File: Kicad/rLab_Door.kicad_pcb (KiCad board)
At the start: 4 copper layers, 100 x 100 mm, 96 parts, among them J1 ACT_1, J10 BATTERY, J11 PROG, J12 PI, J13 TEST POINTS, J2 ACT_2, J3 NPX_1, J4 NPX_2, J5 WIEGAND KEYPAD, J6 NFC SERIAL, J7 I2C DISPLAY, J8 TAMPER, J9 V_IN, Q1 2N7002, Q10 MMBT5551L, Q11 2N7002, Q12 2N7002, Q2 2N7002, Q3 AO3401A, Q4 MMBT5551L, Q5 2N7002, Q6 2N7002, Q7 AO3401A, Q8 2N7002, Q9 2N7002, SW1 RESET, SW2 BOOT, SW3 TEST_1, SW4 TEST_2, U1 MP1584, U2 LM317_TO-252, U3 AMS1117-3.3, U4 ESP32-WROOM-32D

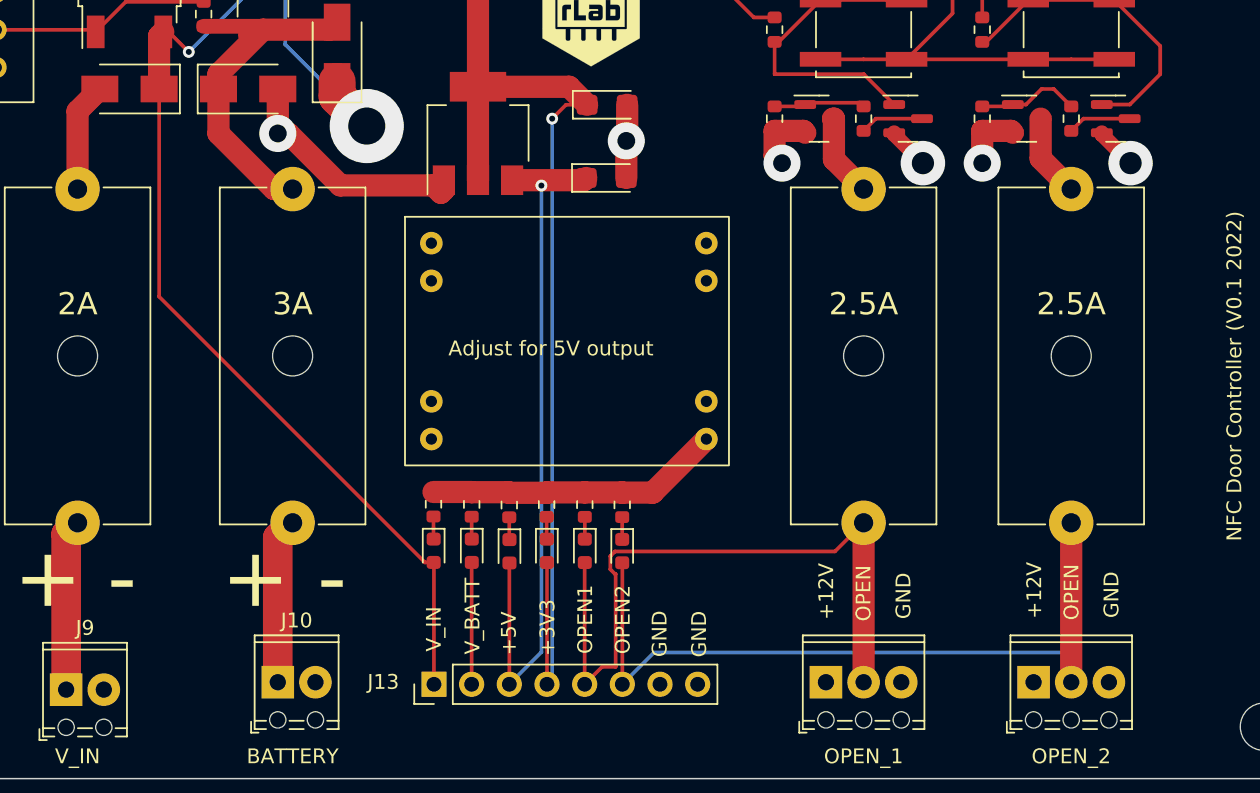
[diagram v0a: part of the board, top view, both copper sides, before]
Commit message: Added some vias to the high power connections to improve current capacity
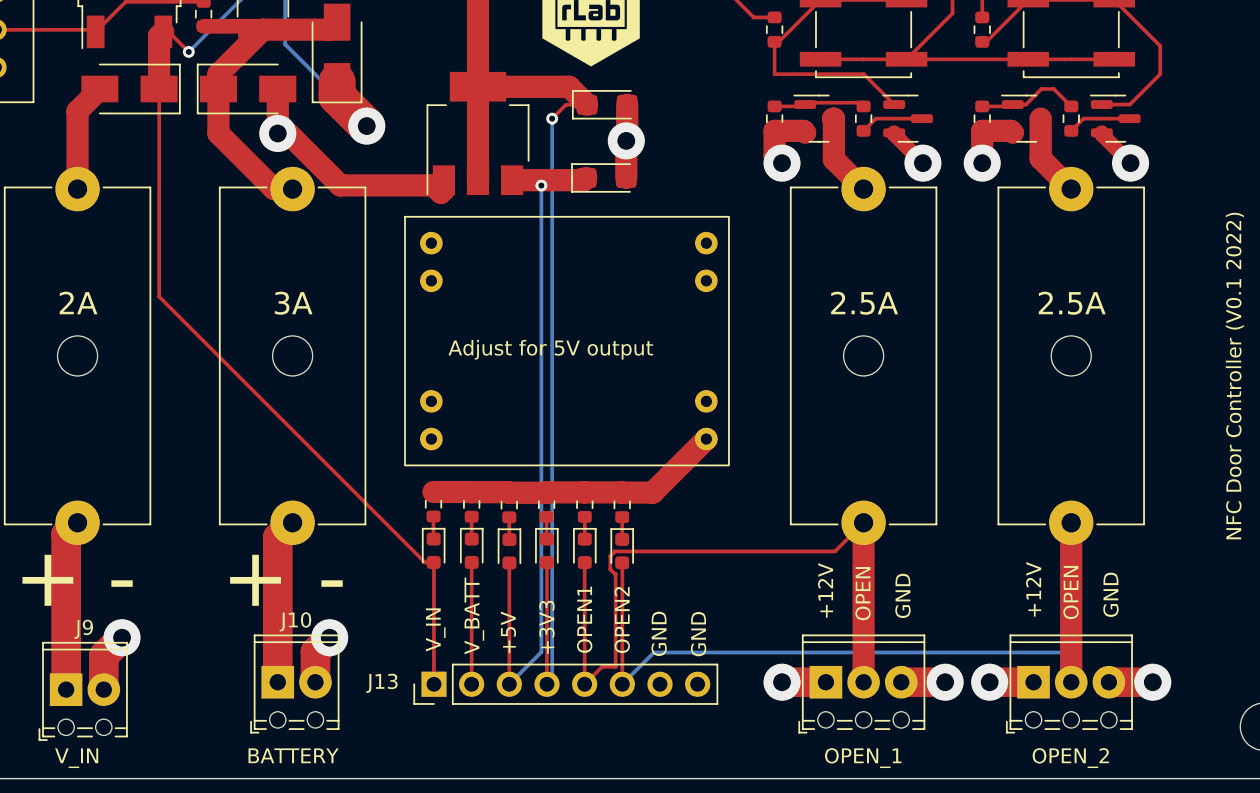
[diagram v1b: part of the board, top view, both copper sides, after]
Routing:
- net GND: track 102.3 -> 115.6 mm, vias 12 -> 16
- net +BATT: track 62.8 -> 68.7 mm, vias 4 -> 6
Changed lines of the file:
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@@
   (segment (start 84.325 67.254176) (end 85.745824 67.254176) (width 0.25) (layer "F.Cu") (net 2))
   (segment (start 89.560842 127.175) (end 89.574391 127.188549) (width 1.5) (layer "F.Cu") (net 2))
+  (segment (start 79.04 137.96) (end 80 137) (width 2) (layer "F.Cu") (net 2))
   (segment (start 76.5 100) (end 76.5 103) (width 1.5) (layer "F.Cu") (net 2))
   (segment (start 100 106) (end 100 103.5) (width 1.5) (layer "F.Cu") (net 2))
@@
   (segment (start 114 56.9) (end 114 59) (width 0.25) (layer "F.Cu") (net 2))
   (segment (start 76.5 103) (end 77.214824 103) (width 1.5) (layer "F.Cu") (net 2))
+  (segment (start 132.54 140) (end 135.5 140) (width 2) (layer "F.Cu") (net 2))
   (segment (start 87.5 107) (end 87.7 106.8) (width 1.5) (layer "F.Cu") (net 2))
   (segment (start 84.25 60.155) (end 88.28 60.155) (width 0.25) (layer "F.Cu") (net 2))
   (segment (start 83.915 59.87) (end 83.94 59.845) (width 0.25) (layer "F.Cu") (net 2))
   (segment (start 91.065 77.665) (end 91.065 75.565) (width 0.25) (layer "F.Cu") (net 2))
+  (segment (start 118.54 140) (end 121.5 140) (width 2) (layer "F.Cu") (net 2))
   (segment (start 100.057332 101.065037) (end 100.057332 103.442668) (width 1.5) (layer "F.Cu") (net 2))
   (segment (start 118.0625 103.0625) (end 120 105) (width 1) (layer "F.Cu") (net 2))
@@
   (segment (start 84.33535 69) (end 86 69) (width 0.25) (layer "F.Cu") (net 2))
   (segment (start 75.835 51.28) (end 75.835 57.08) (width 0.25) (layer "F.Cu") (net 2))
+  (segment (start 64.77 140.5) (end 64.77 138.23) (width 2) (layer "F.Cu") (net 2))
   (segment (start 85.268167 70.768152) (end 85.512299 70.52402) (width 0.25) (layer "F.Cu") (net 2))
   (segment (start 114 59) (end 113 60) (width 0.25) (layer "F.Cu") (net 2))
@@
   (segment (start 99.722911 127.215648) (end 101.786352 127.215648) (width 1.5) (layer "F.Cu") (net 2))
   (segment (start 87 127.175) (end 89.560842 127.175) (width 1.5) (layer "F.Cu") (net 2))
+  (segment (start 79.04 140) (end 79.04 137.96) (width 2) (layer "F.Cu") (net 2))
   (segment (start 99.709362 127.202099) (end 99.722911 127.215648) (width 1.5) (layer "F.Cu") (net 2))
   (segment (start 87 106.5) (end 87.5 107) (width 1.5) (layer "F.Cu") (net 2))
@@
   (segment (start 101.786352 127.215648) (end 105.398 123.604) (width 1.5) (layer "F.Cu") (net 2))
   (segment (start 74.72 51.28) (end 74 52) (width 0.25) (layer "F.Cu") (net 2))
+  (segment (start 64.77 138.23) (end 66 137) (width 2) (layer "F.Cu") (net 2))
   (segment (start 105.28 60.155) (end 112.845 60.155) (width 0.25) (layer "F.Cu") (net 2))
   (segment (start 89.574391 127.188549) (end 92.067485 127.188549) (width 1.5) (layer "F.Cu") (net 2))
@@
   (segment (start 81.94 59.87) (end 80.13 59.87) (width 0.25) (layer "F.Cu") (net 2))
   (segment (start 75.835 58.61) (end 77.225 60) (width 0.25) (layer "F.Cu") (net 2))
+  (via (at 66 137) (size 2.5) (drill 1.2) (layers "F.Cu" "B.Cu") (net 2))
   (via (at 113 60) (size 0.8) (drill 0.4) (layers "F.Cu" "B.Cu") (net 2))
+  (via (at 135.5 140) (size 2.5) (drill 1.2) (layers "F.Cu" "B.Cu") (net 2))
+  (via (at 121.5 140) (size 2.5) (drill 1.2) (layers "F.Cu" "B.Cu") (net 2))
   (via (at 91 75.5) (size 0.8) (drill 0.4) (layers "F.Cu" "B.Cu") (net 2))
   (via (at 86 69) (size 0.8) (drill 0.4) (layers "F.Cu" "B.Cu") (net 2))
   (via (at 74 52) (size 0.8) (drill 0.4) (layers "F.Cu" "B.Cu") (net 2))
-  (via (at 120 105) (size 3) (drill 1.5) (layers "F.Cu" "B.Cu") (net 2))
+  (via (at 120 105) (size 2.5) (drill 1.2) (layers "F.Cu" "B.Cu") (net 2))
   (via (at 86 67) (size 0.8) (drill 0.4) (layers "F.Cu" "B.Cu") (net 2))
   (via (at 85.512299 70.52402) (size 0.8) (drill 0.4) (layers "F.Cu" "B.Cu") (net 2))
   (via (at 80 60) (size 0.8) (drill 0.4) (layers "F.Cu" "B.Cu") (net 2))
-  (via (at 134 105) (size 3) (drill 1.5) (layers "F.Cu" "B.Cu") (net 2))
+  (via (at 134 105) (size 2.5) (drill 1.2) (layers "F.Cu" "B.Cu") (net 2))
+  (via (at 80 137) (size 2.5) (drill 1.2) (layers "F.Cu" "B.Cu") (net 2))
   (via (at 76.5 103) (size 2.5) (drill 1.2) (layers "F.Cu" "B.Cu") (net 2))
   (via (at 100 103.5) (size 2.5) (drill 1.2) (layers "F.Cu" "B.Cu") (net 2))
@@
   (segment (start 125.9375 102.825) (end 126.0625 102.95) (width 1.5) (layer "F.Cu") (net 6))
   (segment (start 110 102.825) (end 111.9375 102.825) (width 1.5) (layer "F.Cu") (net 6))
+  (segment (start 113.46 140) (end 110.5 140) (width 2) (layer "F.Cu") (net 6))
   (segment (start 110 102.825) (end 110 104.5) (width 1.5) (layer "F.Cu") (net 6))
   (segment (start 110 104.5) (end 110.5 105) (width 1.5) (layer "F.Cu") (net 6))
@@
   (segment (start 124 102.825) (end 124 105) (width 1.5) (layer "F.Cu") (net 6))
   (segment (start 89.571669 131.931695) (end 89.571669 140.137882) (width 0.25) (layer "F.Cu") (net 6))
+  (segment (start 127.46 140) (end 124.5 140) (width 2) (layer "F.Cu") (net 6))
   (via (at 77 65.5) (size 0.8) (drill 0.4) (layers "F.Cu" "B.Cu") (net 6))
-  (via (at 82.5 102.5) (size 5) (drill 2.5) (layers "F.Cu" "B.Cu") (net 6))
+  (via (at 82.5 102.5) (size 2.5) (drill 1.2) (layers "F.Cu" "B.Cu") (net 6))
+  (via (at 110.5 140) (size 2.5) (drill 1.2) (layers "F.Cu" "B.Cu") (net 6))
   (via (at 124 105) (size 2.5) (drill 1.2) (layers "F.Cu" "B.Cu") (net 6))
   (via (at 110.5 105) (size 2.5) (drill 1.2) (layers "F.Cu" "B.Cu") (net 6))
+  (via (at 124.5 140) (size 2.5) (drill 1.2) (layers "F.Cu" "B.Cu") (net 6))
   (segment (start 77 97) (end 82.5 102.5) (width 0.25) (layer "B.Cu") (net 6))
   (segment (start 77 65.5) (end 77 97) (width 0.25) (layer "B.Cu") (net 6))
